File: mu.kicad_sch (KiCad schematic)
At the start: 54 parts, among them U1 STM32F042F6P6, U11 MICROFC-60035-SMT-TR1, U12 TLV3601DCKT, U13 OPA656NB/250, U2 MAX5026EUT_T, U3 MCP4921-E/SN, U4 LM4040AIM3-2.5/NOPB, U5 W25Q128JVS, U6 TLV70433DBVT, U7 SN74LVC1G74DCUT, U8 sn65hvd230, U9 LT3045xDD

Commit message: added usb c and fixed many silly issues
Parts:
- removed U12: TLV3601DCKT, SC_601DCKT_TEX, symbol TLV3601DCKT:TLV3601DCKT
- added C27: 10uF, Capacitor_SMD:C_0402_1005Metric, symbol Device:C_Polarized
- added C28: 100nF, Resistor_SMD:R_0402_1005Metric, symbol Device:C
- added D1: BAT54C, Package_TO_SOT_SMD:SOT-23, symbol Diode:BAT54C
- added J1: USB4105-GF-A, USB4105-GF-A:GCT_USB4105-GF-A, symbol USB4105-GF-A:USB4105-GF-A
- added J2: Conn_02x03_Odd_Even, symbol Connector_Generic:Conn_02x03_Odd_Even
- added R13, R14: 5.1K, Resistor_SMD:R_0402_1005Metric, symbol Device:R
- added R15, R16: 10K, Resistor_SMD:R_0402_1005Metric, symbol Device:R
- added R9: 100kΩ, Resistor_SMD:R_0402_1005Metric, symbol Device:R
- added U10: TLV3603QDCKRQ1, SC70_PLV3603_TEX, symbol TLV3603:TLV3603QDCKRQ1
- C11: value 1uF -> 100nF; footprint Capacitor_SMD:C_0402_1005Metric -> Resistor_SMD:R_0402_1005Metric
- R1: value 158.5K -> 147K
- R8: now not fitted
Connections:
- net 2.5V_Ref: no longer U3.6 (VREFA)
- net 3.3V_Dig: no longer C10.1, C12.1, C19.1, C20.1, U3.1 (VDD), U7.2 (D), U7.8 (VCC)
- net 5V: now also C10.1, C12.1, C19.1, C20.1, U3.1 (VDD), U3.6 (VREFA), U7.2 (D), U7.8 (VCC), C27.1, C28.1, U10.6 (VCC)
- net BAT+: now also D1.1; no longer C11.2, U6.2 (IN)
- net CAN_rx: now also J2.1 (Pin_1); no longer U1.17 (PA9/PA11)
- net CAN_tx: now also J2.2 (Pin_2); no longer U1.18 (PA10/PA12)
- net DAC_out: now also C23.1, U10.4 (IN-); no longer C23.2
- net GND: now also C23.2, C27.2, C28.2, J1.A1_B12 (GND), J1.B1_A12 (GND), J1.SH1 (SHELL_GND), J1.SH2 (SHELL_GND), J1.SH3 (SHELL_GND), J1.SH4 (SHELL_GND), R13.2, R14.1, R16.1, R9.1, U10.2 (VEE); no longer C23.1
- net at C4.1, C4.2, RF1.2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: now also U10.3 (IN+)
- net Mode_sel: now reaches U1.6 (PA0)
- net Mode_sel: now also R15.1, R16.2
- net SPI_CS_FLASH: now reaches U1.9 (PA3)
- net SPI_CS_FLASH: now also U5.1 (~{CS})
- net at U7.1 (CLK): now also U10.1 (OUT)
- net SPI_CS renamed SPI_CS_DAC
- net SPI_CS_DAC: no longer U5.1 (~{CS})
- new net: R9.2, U10.5 (LE/HYS)
- new net: C11.2, D1.3, U6.2 (IN)
- new net: J1.A5 (CC1), R14.2
- new net: J1.B5 (CC2), R13.1
- new net PA11: J2.3 (Pin_3), U1.17 (PA9/PA11)
- new net PA12: J2.4 (Pin_4), U1.18 (PA10/PA12)
- new net USB_DN: J1.A7 (DN1), J1.B7 (DN2), J2.5 (Pin_5)
- new net USB_DP: J1.A6 (DP1), J1.B6 (DP2), J2.6 (Pin_6)
- new net VBUS: D1.2, J1.A4_B9 (VBUS), J1.B4_A9 (VBUS), R15.2
- no-connect marks 4 -> 9
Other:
- note added: "USB-C & mode select"
- note removed: "hysteresis resistor?"
- note removed: "must increase the output voltage by the expected drop along the rc filter. also need to know exactly what biasing voltage we need for the SiPM we end up choosing. I guess we are going with hamamatsu given what they've been doing for us. Need to update feedback resistors once we figure that out. Bias+virtual_ground+expected drop ==is what we need the switching regulator to be outputting"
- note removed: "need to check these resistor values, currently they are 6.65k and 154k"
- moved on the sheet: C21, C22, C23, C24, R11, R12, R6, U1A, U5, U8

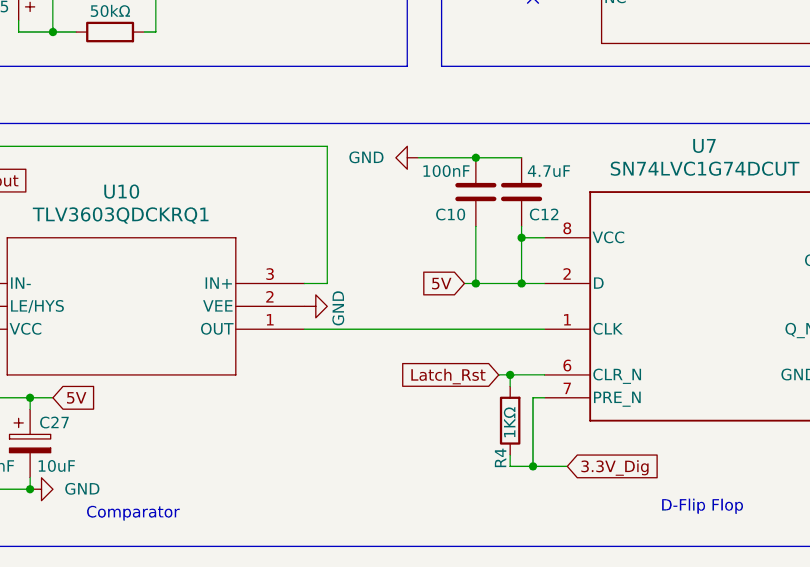
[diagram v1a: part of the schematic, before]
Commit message: flipflop is 3v3
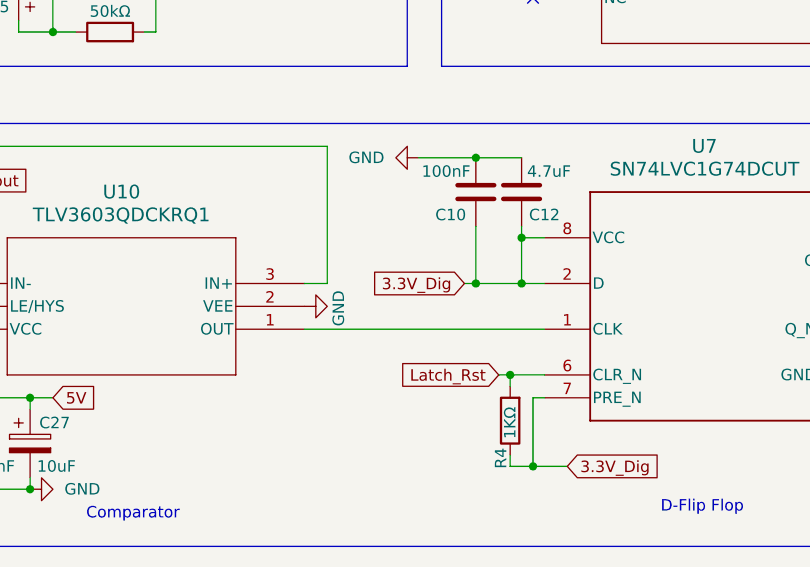
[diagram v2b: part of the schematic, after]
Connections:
- net 3.3V_Dig: now also C10.1, C12.1, U7.2 (D), U7.8 (VCC)
- net 5V: no longer C10.1, C12.1, U7.2 (D), U7.8 (VCC)

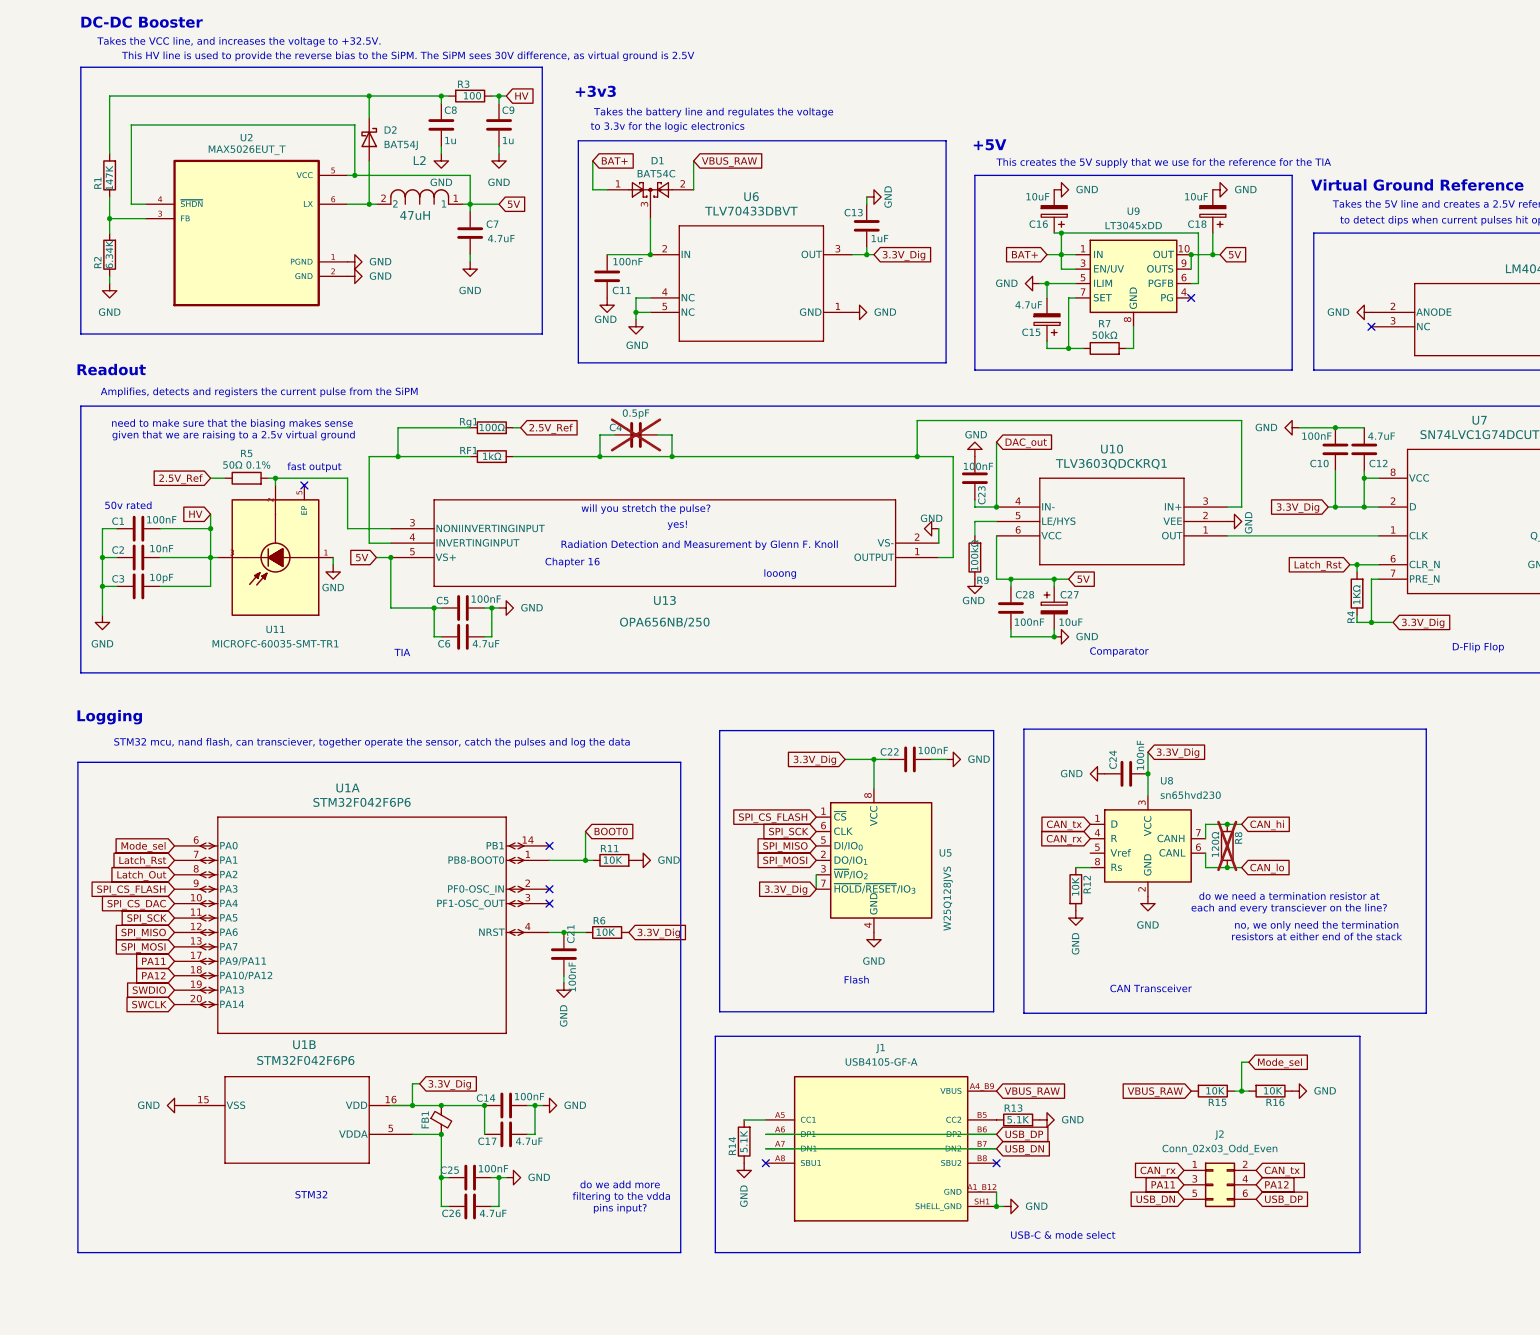
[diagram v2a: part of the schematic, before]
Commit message: esd protection
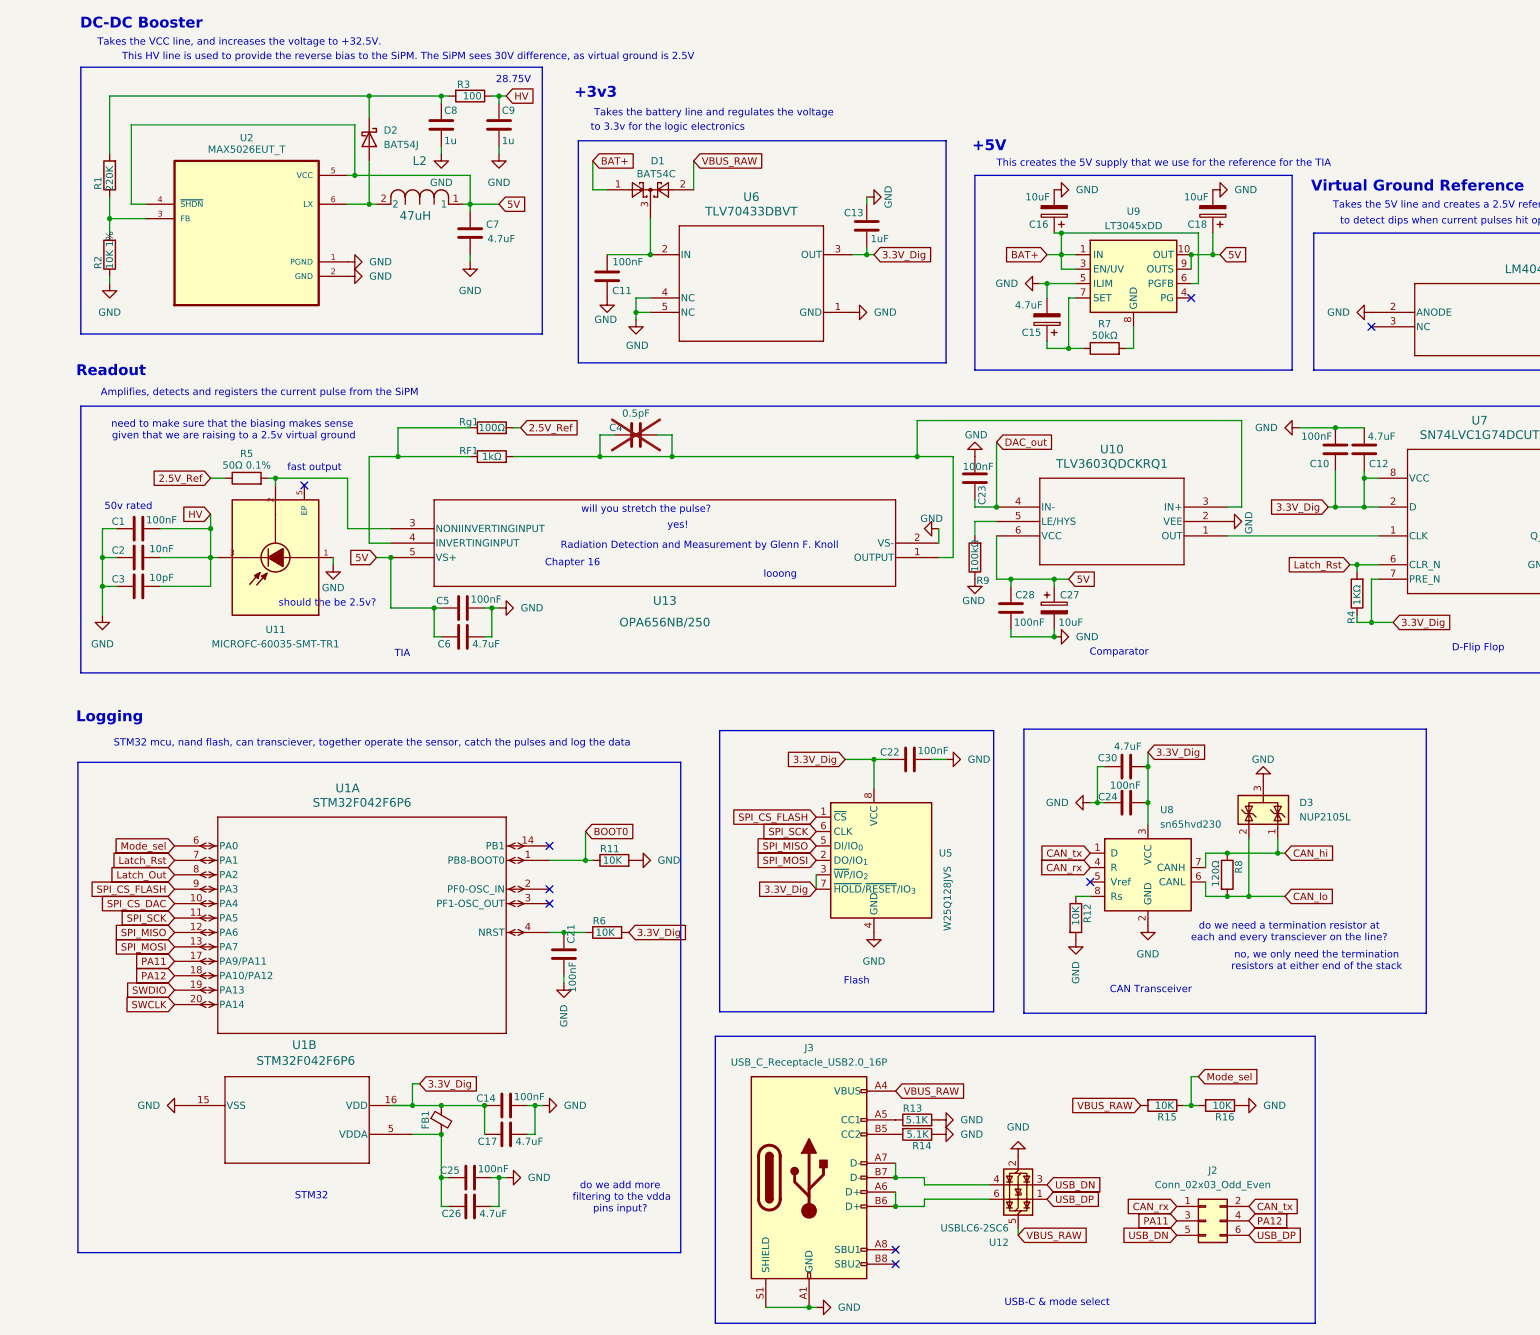
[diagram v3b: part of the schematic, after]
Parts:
- removed J1: USB4105-GF-A, USB4105-GF-A:GCT_USB4105-GF-A, symbol USB4105-GF-A:USB4105-GF-A
- added C30: 4.7uF, Capacitor_SMD:C_0402_1005Metric, symbol Device:C
- added D3: NUP2105L, Package_TO_SOT_SMD:SOT-23, symbol Power_Protection:NUP2105L
- added J3: USB_C_Receptacle_USB2.0_16P, Connector_USB:USB_C_Receptacle_G-Switch_GT-USB-7010ASV, symbol Connector:USB_C_Receptacle_USB2.0_16P
- added U12: USBLC6-2SC6, Package_TO_SOT_SMD:SOT-23-6, symbol Power_Protection:USBLC6-2SC6
- J2: footprint (none) -> Connector_PinHeader_1.00mm:PinHeader_2x03_P1.00mm_Vertical
- R1: value 147K -> 220K
- R2: value 6.34K -> 10K 1%
- R8: now fitted
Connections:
- net 3.3V_Dig: now also C30.2
- net CAN_hi: now also D3.1 (K)
- net CAN_lo: now also D3.2 (K)
- net GND: now also C30.1, D3.3 (A), J3.A1 (GND), J3.A12 (GND), J3.B1 (GND), J3.B12 (GND), J3.S1 (SHIELD), U12.2 (GND)
- net USB_DN: now also U12.3 (I/O2)
- net USB_DP: now also U12.1 (I/O1)
- net at R14.2: now also J3.B5 (CC2)
- net at R13.1: now also J3.A5 (CC1)
- net VBUS renamed VBUS_RAW
- net VBUS_RAW: now also J3.A4 (VBUS), J3.A9 (VBUS), J3.B4 (VBUS), J3.B9 (VBUS), U12.5 (VBUS)
- new net: J3.A7 (D-), J3.B7 (D-), U12.4 (I/O2)
- new net: J3.A6 (D+), J3.B6 (D+), U12.6 (I/O1)
- no-connect marks 9 -> 10
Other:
- note added: "28.75V"
- note added: "should the be 2.5v?"
- moved on the sheet: C24, J2, R12, R13, R14, R15, R16, U8

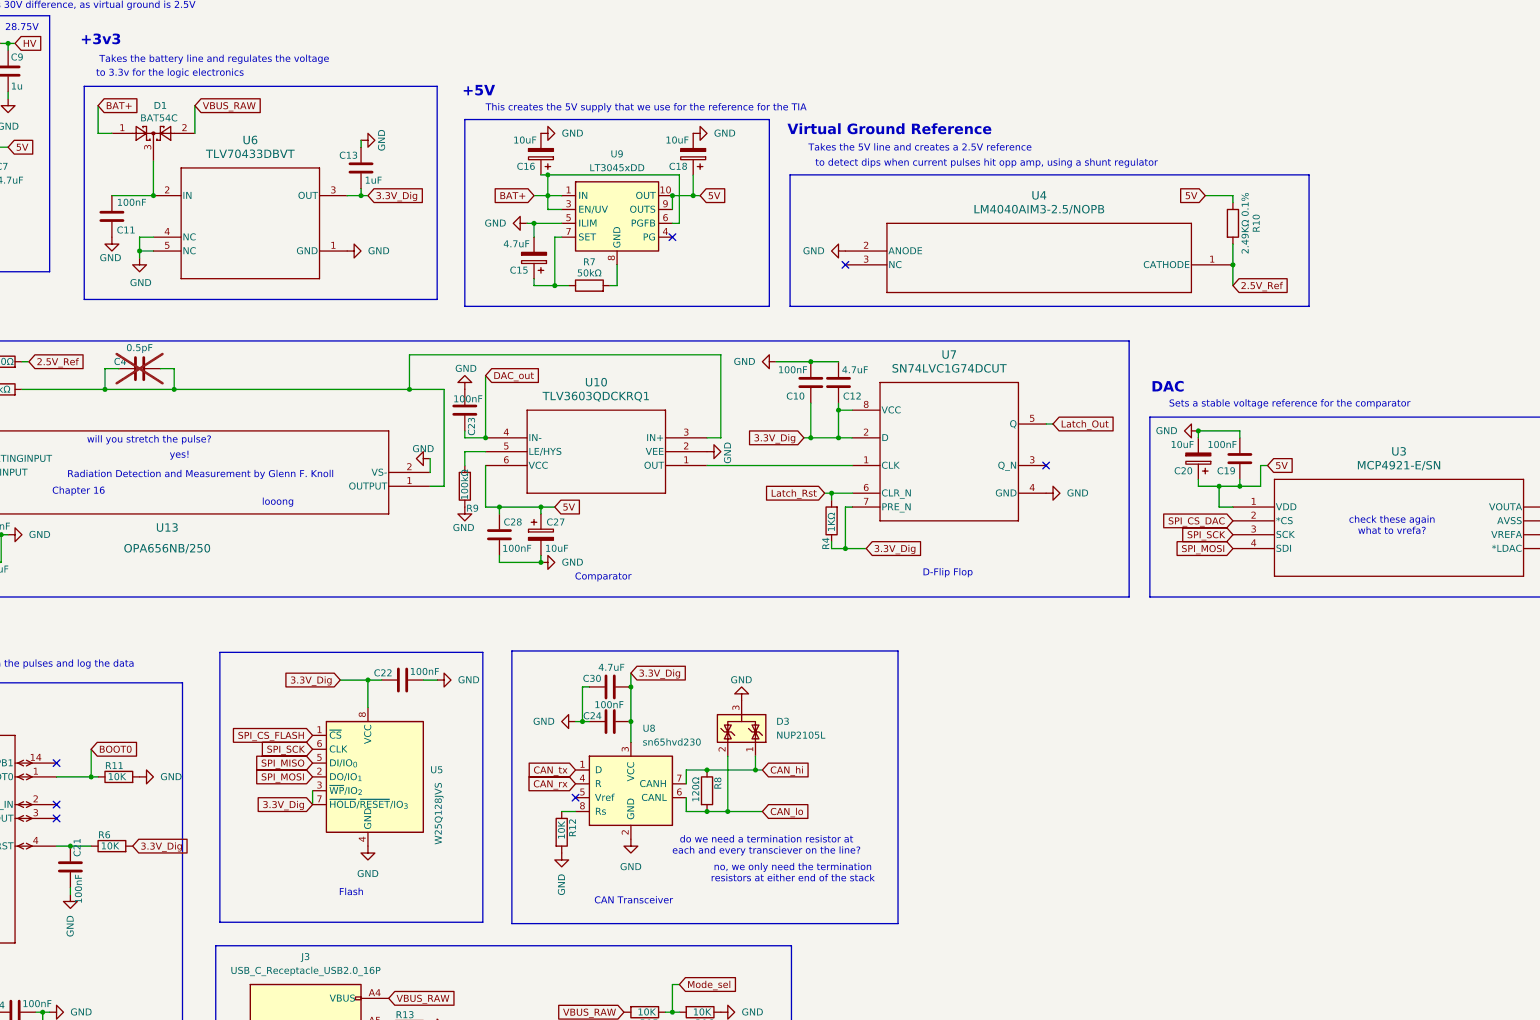
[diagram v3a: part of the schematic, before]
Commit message: schematic locked in, connenctors added
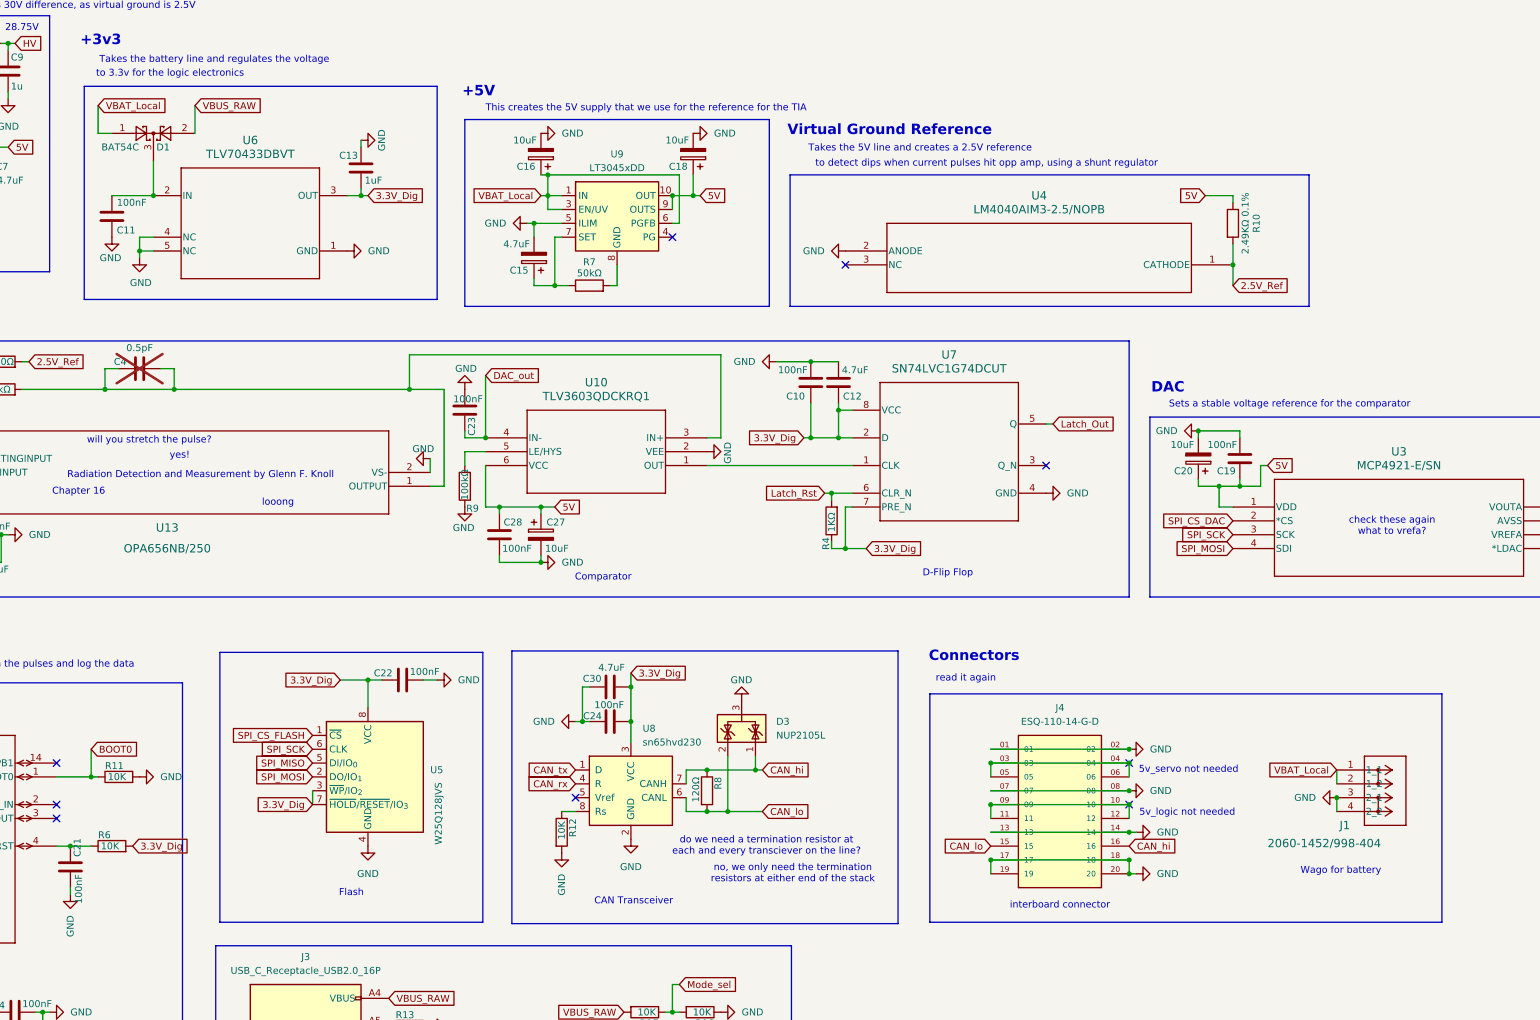
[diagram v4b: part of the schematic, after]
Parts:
- added J1: 2060-1452/998-404, CONN2_2060-1452/998-404_WAG, symbol Wago 2060-1452 998-404:2060-1452_998-404
- added J4: ESQ-110-14-G-D, ESQ-110-X-X-D:ESQ-110-X-X-D, symbol ESQ-110-X-X-D:ESQ-110-X-X-D
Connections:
- net CAN_hi: now also J4.16
- net CAN_lo: now also J4.15
- net GND: now also J1.3 (2_1), J1.4 (2_2), J4.01, J4.02, J4.07, J4.08, J4.13, J4.14, J4.17, J4.18, J4.19, J4.20
- net BAT+ renamed VBAT_Local
- net VBAT_Local: now also J1.1 (1_1), J1.2 (1_2)
- new net: J4.03, J4.04, J4.05, J4.06
- new net: J4.09, J4.10, J4.11, J4.12
- no-connect marks 10 -> 12
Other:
- note added: "5v_logic not needed"
- note added: "5v_servo not needed"
- note added: "Connectors"
- note added: "Wago for battery"
- note added: "interboard connector"
- note added: "read it again"
